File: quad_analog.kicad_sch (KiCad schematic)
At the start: 24 parts, among them U21 MCP6004, U22 SRV05-4

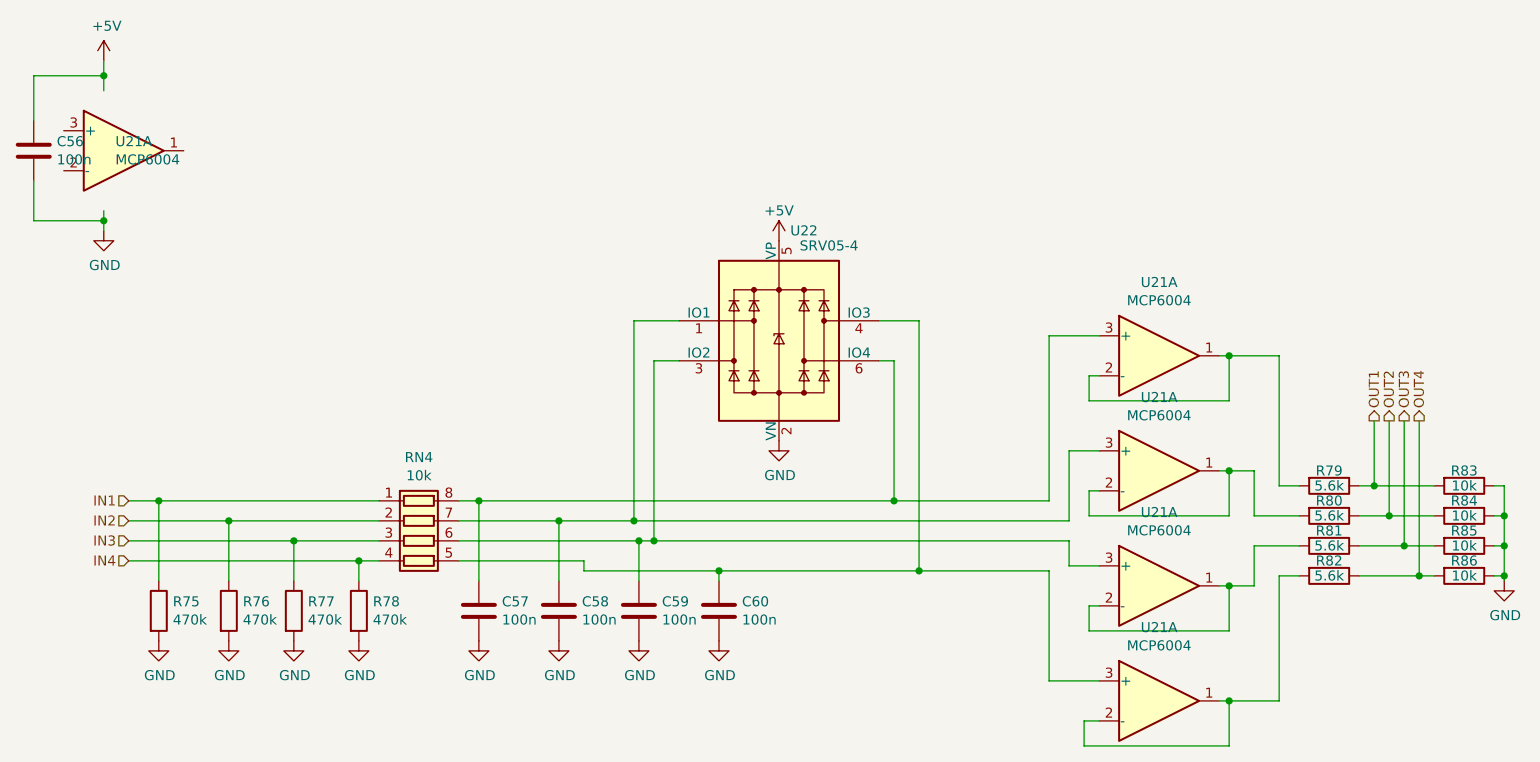
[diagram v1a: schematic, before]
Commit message: Published 1.5 gerbs, bom, cpl and pdf
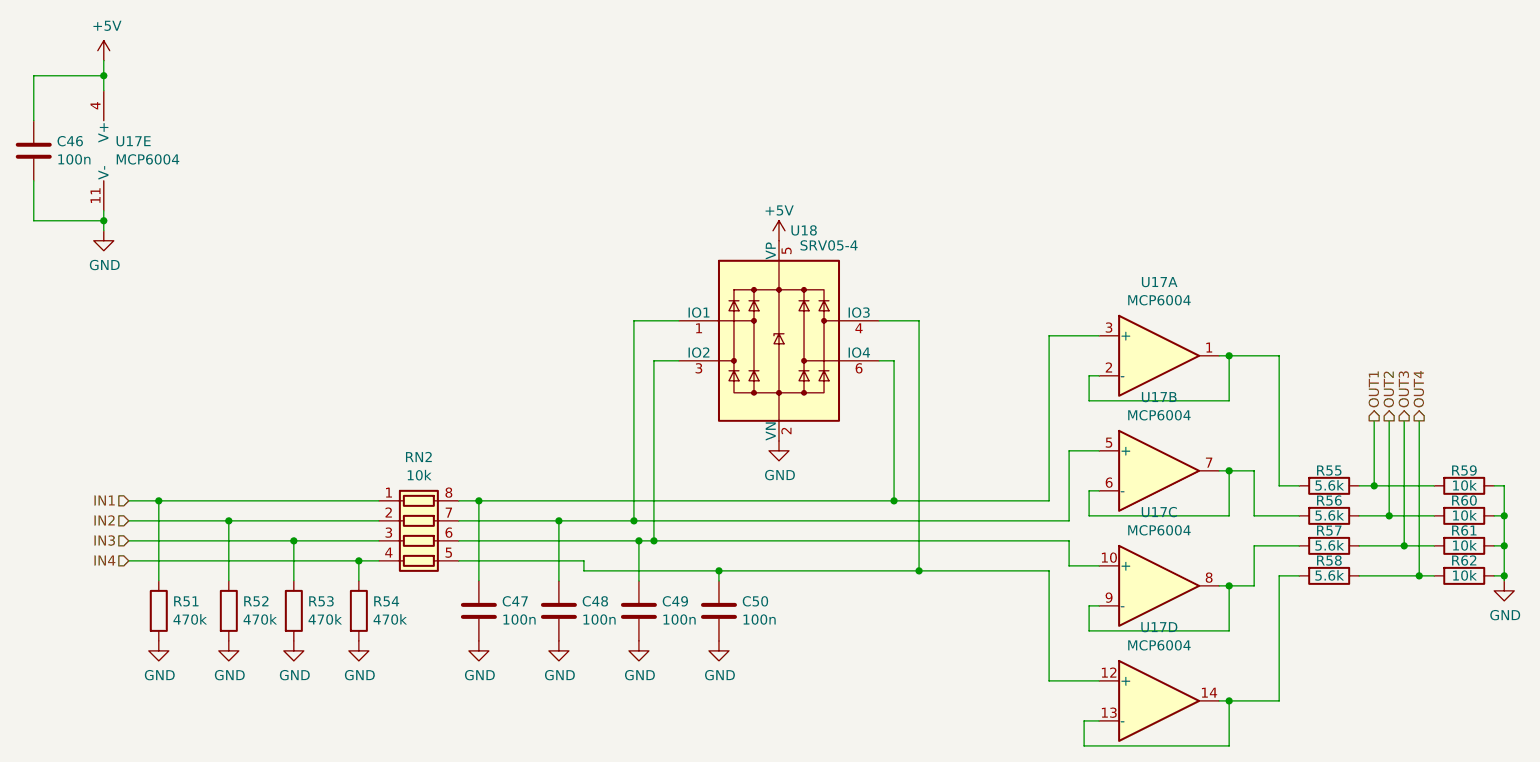
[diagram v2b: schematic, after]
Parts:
- renumbered C56 to C46, C57 to C47, C58 to C48, C59 to C49, C60 to C50, R75 to R51, R76 to R52, R77 to R53, R78 to R54, R79 to R55, R80 to R56, R81 to R57, R82 to R58, R83 to R59, R84 to R60, R85 to R61, R86 to R62, RN4 to RN2, U21 to U17, U22 to U18
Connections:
- net +5V: now also U17.4 (V+)
- net GND: now also U17.11 (V-)
- net at C48.1, RN2.7 (R2.2), U18.1 (IO1): now also U17.5 (+); no longer U17.3 (+)
- net at C49.1, RN2.6 (R3.2), U18.3 (IO2): now also U17.10 (+); no longer U17.3 (+)
- net at C50.1, RN2.5 (R4.2), U18.4 (IO3): now also U17.12 (+); no longer U17.3 (+)
- new net: R56.2, U17.6 (-), U17.7
- new net: R57.2, U17.8, U17.9 (-)
- new net: R58.2, U17.13 (-), U17.14
